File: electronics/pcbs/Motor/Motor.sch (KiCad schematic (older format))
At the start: 13 parts, among them P1 Digital, P10 CONN_01X01, P11 CONN_01X01, P12 CONN_01X01, P13 CONN_01X01, P2 Power, P3 Analog, P4 Analog, P5 PWM, P6 PWM, P7 Communication, P8 CONN_01X01, P9 CONN_01X01

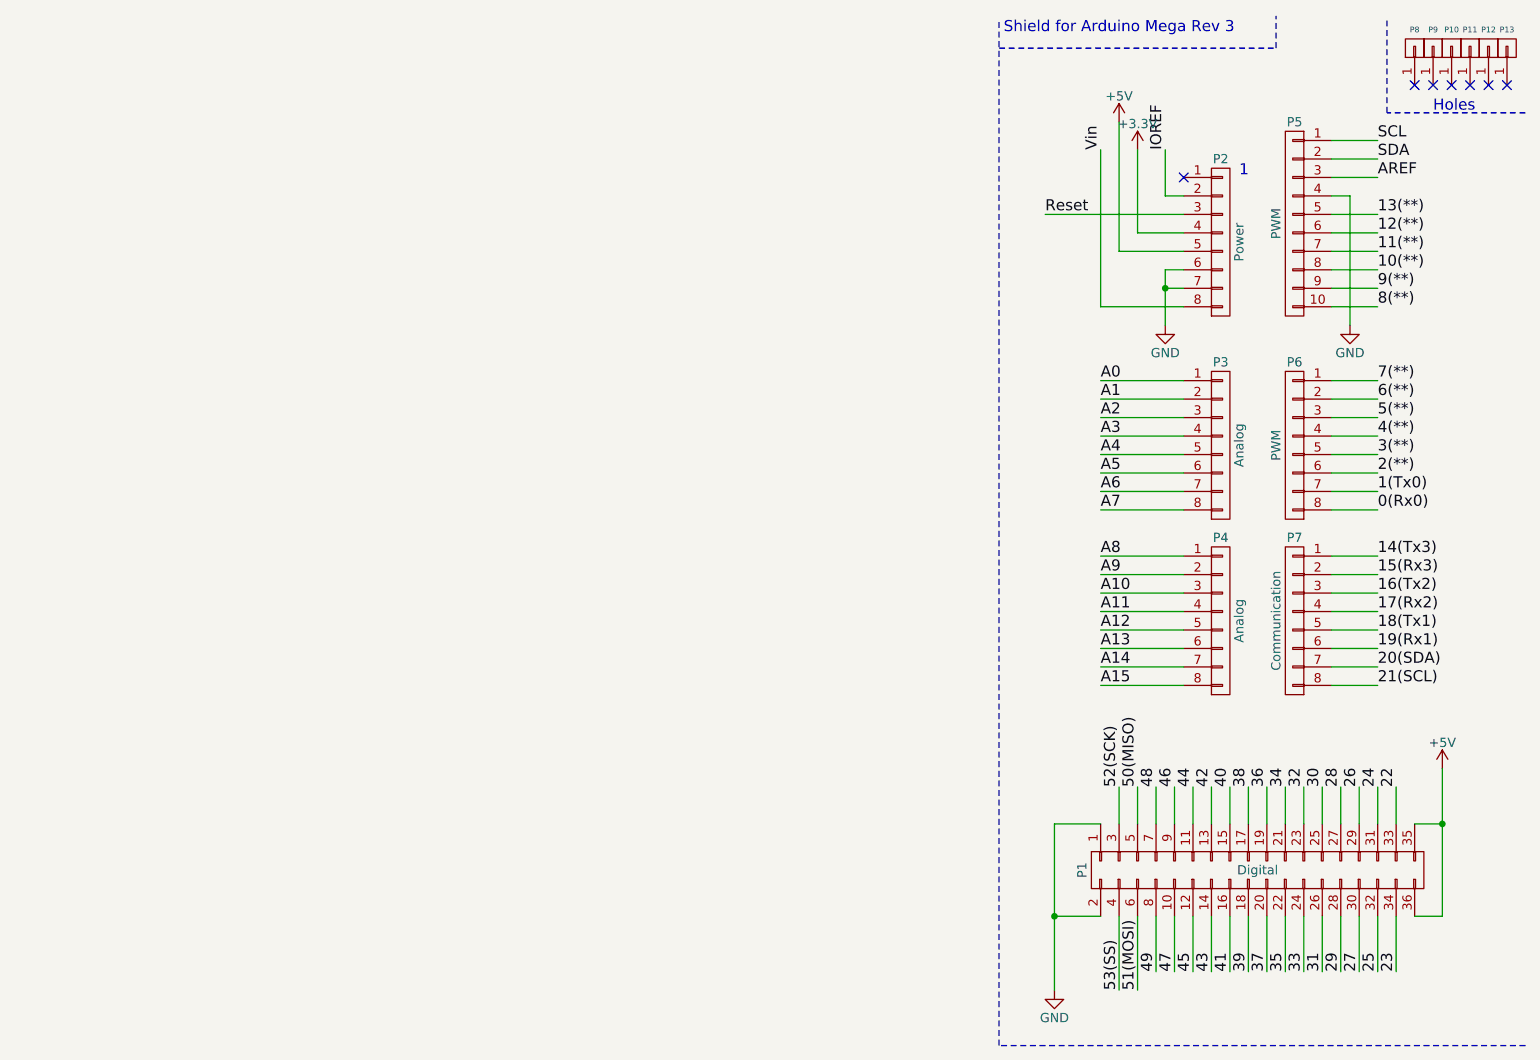
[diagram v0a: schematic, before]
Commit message: Motor PCB: Redesigned schematic for the Mega.
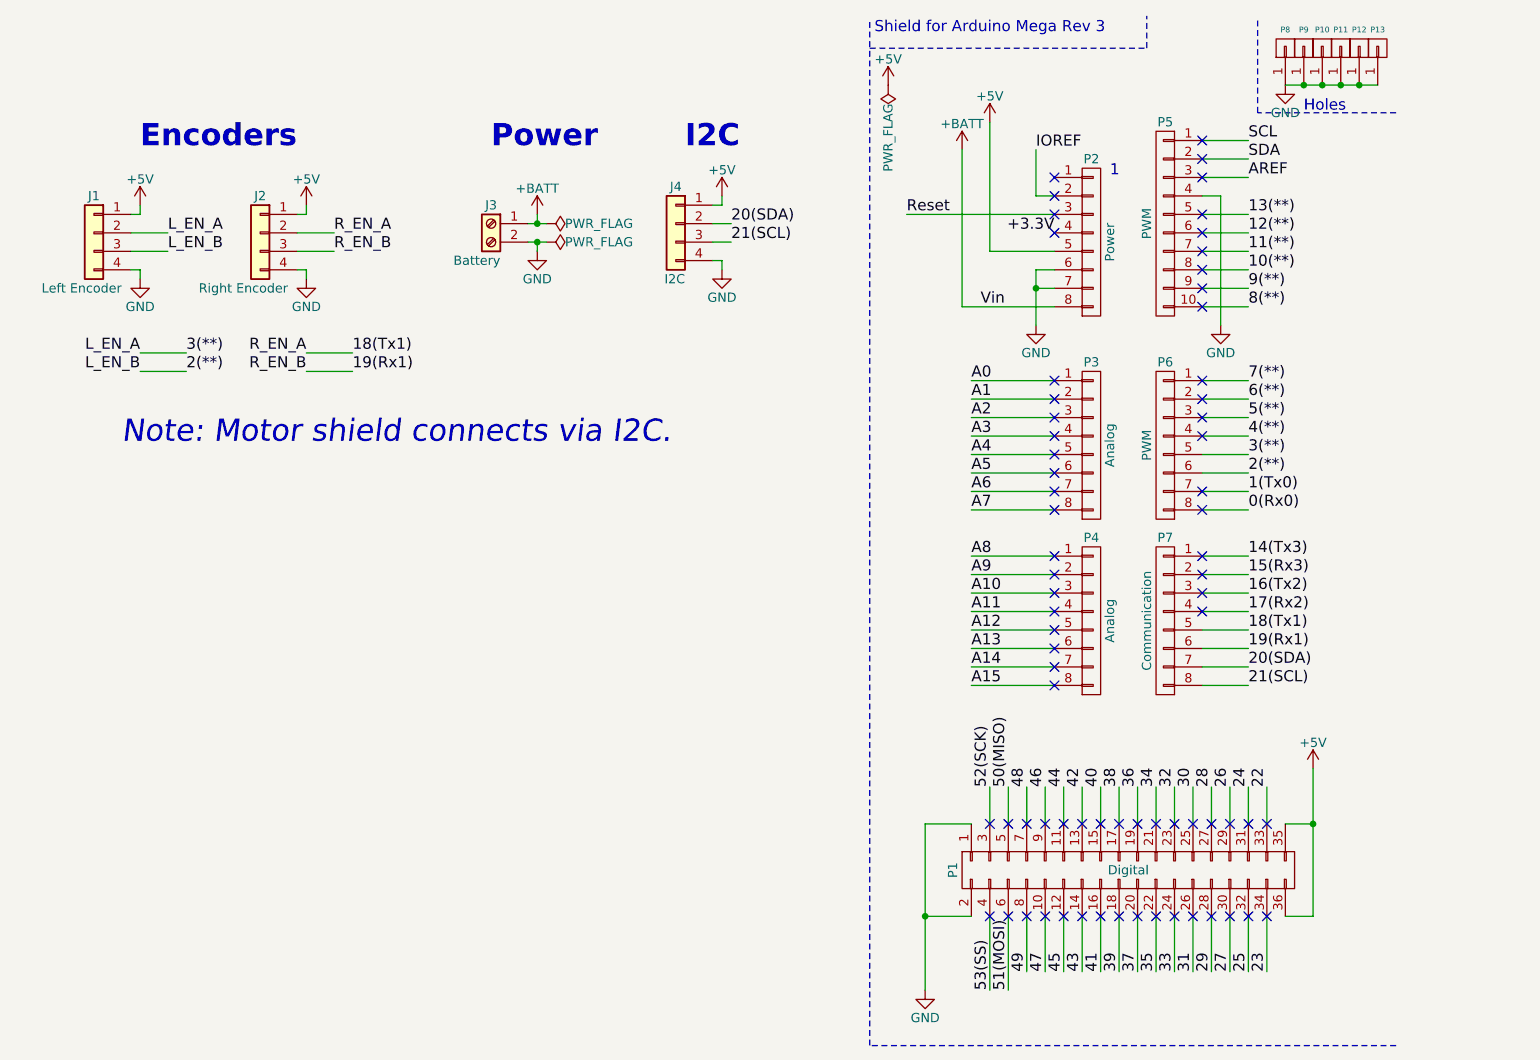
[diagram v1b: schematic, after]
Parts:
- added J1: Left Encoder, Connectors_Samtec:SL-104-X-XX_1x04, symbol Conn_01x04
- added J2: Right Encoder, Connectors_Samtec:SL-104-X-XX_1x04, symbol Conn_01x04
- added J3: Battery, Connectors_Terminal_Blocks:TerminalBlock_bornier-2_P5.08mm, symbol Screw_Terminal_01x02
- added J4: I2C, Connectors_Samtec:SL-104-X-XX_1x04, symbol Conn_01x04
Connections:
- net +5V: now also J1.1 (Pin_1), J2.1 (Pin_1), J4.1 (Pin_1)
- net 18(Tx1): now also J2.2 (Pin_2)
- net 19(Rx1): now also J2.3 (Pin_3)
- net 2(**): now also J1.3 (Pin_3)
- net 20(SDA): now also J4.2 (Pin_2)
- net 21(SCL): now also J4.3 (Pin_3)
- net 3(**): now also J1.2 (Pin_2)
- net GND: now also P10.1 (P1), P11.1 (P1), P12.1 (P1), P13.1 (P1), P8.1 (P1), P9.1 (P1), J1.4 (Pin_4), J2.4 (Pin_4), J3.2 (Pin_2), J4.4 (Pin_4)
- net +3V3 renamed +3.3V
- net Vin renamed +BATT
- net +BATT: now also J3.1 (Pin_1)
- no-connect marks 7 -> 71
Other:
- note added: "Encoders"
- note added: "I2C"
- note added: "Note: Motor shield connects via I2C."
- note added: "Power"
- moved on the sheet: P1, P10, P11, P12, P13, P2, P3, P4, P5, P6, P7, P8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
